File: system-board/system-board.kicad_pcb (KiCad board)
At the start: 4 copper layers, 50 x 17.5 mm, 69 parts, among them IC1 Flash_16Mb, IC2 LSM6DSLTR, IC3 AP2115M-3.3TRG1, J1 BATT, J10 217183-0001, J2 GTFP08431BEU, J3 QWIIC, J4 SPKR, J5 BLADE_1, J6 BLADE_2, J7 BLADE_3, J8 BLADE_4, J9 BTNS, Q1 DMP1012UFDF, Q2 SSM6K504NU.LF, Q3 SSM6K504NU.LF, Q4 DMP1012UFDF, Q5 PMZB290UNE2YL, Q6 PMZB290UNE2YL, Q7 PMZB290UNE2YL, Q8 PMZB290UNE2YL, SW1 RST, SW2 USR, U1 MDBT50Q-1MV2, U2 MAX98357AETE+T, U3 BQ29705DSER, U4 MCP73832-2-OT, Y1 32.768k

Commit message: First attempt
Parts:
- removed J5: BLADE_1, Connector_JST:JST_SH_SM02B-SRSS-TB_1x02-1MP_P1.00mm_Horizontal
- removed J6: BLADE_2, Connector_JST:JST_SH_SM02B-SRSS-TB_1x02-1MP_P1.00mm_Horizontal
- removed J7: BLADE_3, Connector_JST:JST_SH_SM02B-SRSS-TB_1x02-1MP_P1.00mm_Horizontal
- removed J8: BLADE_4, Connector_JST:JST_SH_SM02B-SRSS-TB_1x02-1MP_P1.00mm_Horizontal
- added J11: 503398-1892, Imports:Molex uSD Card Holder Push-Push 503398-1892, B.Cu at (116.8, 91.4)
- C1, C2, C3, C4, C5, C6, C7, C8, FB1, FB2, R1, R2, R7, U1, Y1: moved to B.Cu
- D1: value WS2812B -> WS2812B-2020
- IC2, J3, R5, R6: moved to F.Cu
- J2: value GTFP08431BEU -> LEDs; footprint Imports:GTFP08431BEU -> Connector_PinSocket_2.00mm:PinSocket_2x04_P2.00mm_Vertical; moved to F.Cu
- J4: footprint Connector_JST:JST_SH_SM02B-SRSS-TB_1x02-1MP_P1.00mm_Horizontal -> Connector_PinSocket_2.00mm:PinSocket_1x02_P2.00mm_Vertical
- J9: value BTNS -> BTNs; footprint Connector_JST:JST_SH_SM05B-SRSS-TB_1x05-1MP_P1.00mm_Horizontal -> Connector_PinSocket_2.00mm:PinSocket_2x03_P2.00mm_Vertical; moved to F.Cu
- U2: footprint MaximCustom:Maxim_Integrated-T1633-4-0-V-IPC_C -> Imports:Maxim_Integrated-T1633-4-0-V-IPC_C; moved to B.Cu
- moved J3 44.4 mm to (72.2, 98.2), turned to -90 degrees
- moved R6 42.5 mm to (76.3, 101.1), turned to -90 degrees
- moved R5 40.2 mm to (76.3, 98.2), turned to -90 degrees
- moved C6 36.8 mm to (82.6, 95.0), turned to 90 degrees
- moved J4 34.5 mm to (83.2, 92.6)
- moved FB2 33.4 mm to (84.5, 94.8), turned to 0 degrees
- moved Q5 31.5 mm to (85.1, 99.9), turned to -90 degrees
- moved FB1 30.5 mm to (88.2, 91.8), turned to 0 degrees
- moved C5 30.4 mm to (87.6, 93.1), turned to 180 degrees
- moved IC3 28.7 mm to (79.6, 100.8), turned to -90 degrees
- moved R15 25.3 mm to (79.6, 105.0), turned to 180 degrees
- moved C11 25.2 mm to (82.0, 105.3)
- moved SW1 24.8 mm to (70.1, 92.8), turned to 0 degrees
- moved Q6 23.7 mm to (87.1, 99.9), turned to -90 degrees
- moved C12 23.3 mm to (83.1, 98.0), turned to -90 degrees
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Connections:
- J2 pad 1: unconnected-(J2-DAT2-Pad1) -> /Blade LED Out/Blade_1_Out
- J2 pad 2: GND -> VDD
- J2 pad 3: /MOSI -> /Blade LED Out/Blade_2_Out
- J2 pad 4: VCC -> VDD
- J2 pad 5: /SCK -> /Blade LED Out/Blade_3_Out
- J2 pad 6: GND -> VDD
- J2 pad 7: /MISO -> /Blade LED Out/Blade_4_Out
- J2 pad 8: unconnected-(J2-DAT1-Pad8) -> VDD
- J9 pad 2: /A0 -> GND
- J9 pad 3: Net-(J9-Pin_3) -> /A0
- J9 pad 4: Net-(J9-Pin_4) -> /A2
- J9 pad 5: /A2 -> Net-(J9-Pin_5)
- R21 pad 1: Net-(J9-Pin_3) -> Net-(J9-Pin_5)
- R22 pad 1: Net-(J9-Pin_4) -> Net-(J9-Pin_6)
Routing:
- net /D10: track 54.1 -> 0.00 mm, vias 3 -> 0
- net /D9: track 47.4 -> 0.00 mm, vias 1 -> 0
- net /SCL: track 49.1 -> 4.41 mm, vias 3 -> 1
- net /SDA: track 48.1 -> 5.53 mm
- net /D6: track 36.1 -> 0.00 mm, vias 1 -> 0
- net /D5: track 35.7 -> 0.00 mm, vias 1 -> 0
- net /CONN_USB_D+: track 24.4 -> 50.0 mm, vias 2 -> 1
- net /CONN_USB_D-: track 24.6 -> 48.3 mm, vias 2 -> 1
- net /A0: track 21.7 -> 0.00 mm, vias 1 -> 0
- net /Power Management/BATT_PROT_+: track 4.20 -> 25.2 mm
- net /VDIV: track 40.1 -> 20.0 mm, vias 2 -> 1
- net /Power Management/VBUS: track 51.6 -> 69.6 mm, vias 3 -> 5
- net GND: track 107.9 -> 90.6 mm, vias 34 -> 30
- net Net-(J10-CC2): track 0.89 -> 16.0 mm, vias 0 -> 1
- net /A4: track 28.5 -> 15.6 mm, vias 2 -> 1
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- removed copper zone on F.Cu, net /Power Management/BATT_PROT_+
- removed copper zone on F.Cu, net /Power Management/BATT_RAW_+
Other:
- board size 50 x 17.5 mm -> 50 x 15 mm
- board text removed: "+"
- board text removed: "-"

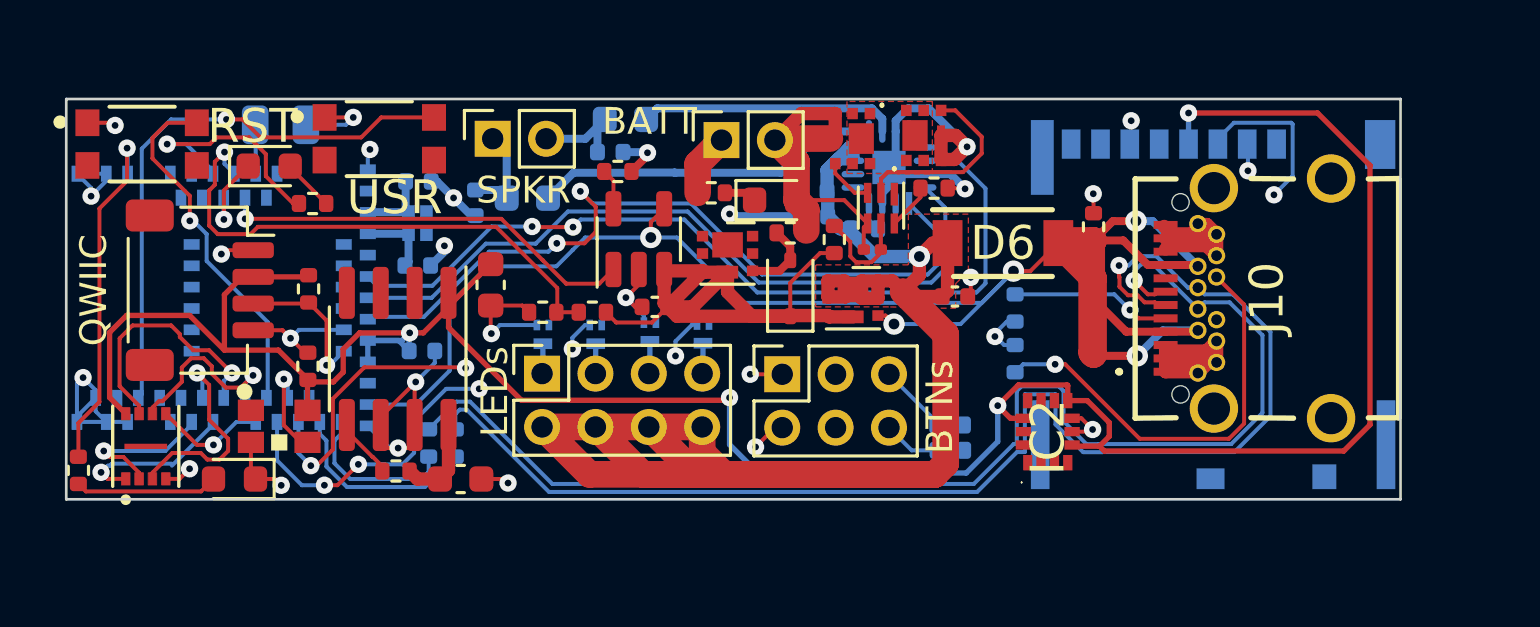
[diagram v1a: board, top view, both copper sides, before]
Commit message: Redo system-board PCB to use fewer connectors
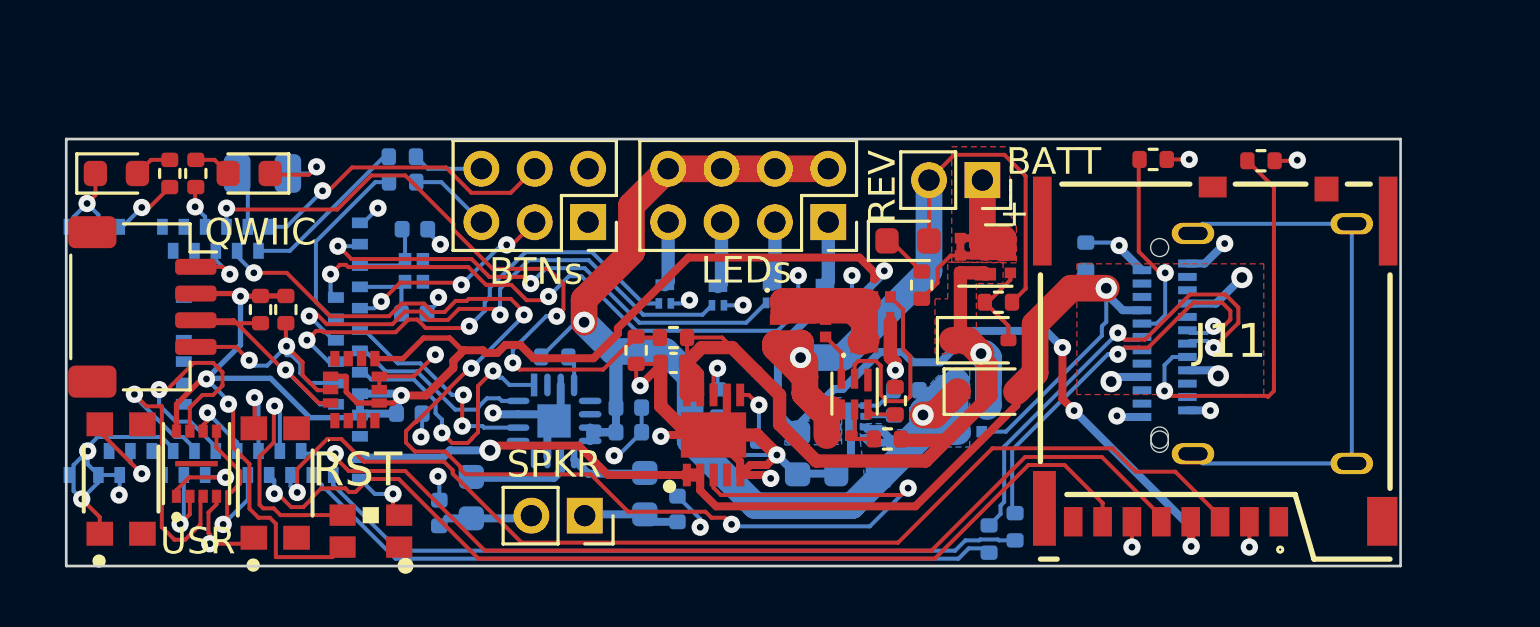
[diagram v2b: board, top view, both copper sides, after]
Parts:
- removed J10: 217183-0001, Imports:Molex USB-C Horizontal 2171830001
- removed U4: MCP73832-2-OT, Package_TO_SOT_SMD:SOT-23-5
- added IC4: MCP73834T-FCI_MF, Imports:SON50P300X300X100-11N-D, F.Cu at (91.5, 103.7)
- added J5: 105450-0101, Imports:AMPHENOL_12401832E402A, B.Cu at (108.2, 100.2)
- added R17: 10k, Resistor_SMD:R_0402_1005Metric, B.Cu at (91.7, 102.5)
- C11, C12, C15, Q4, R11, R15, R16: moved to B.Cu
- D6: value RSX501LAM20TR -> PMEG1030EJ; footprint Imports:SODFL4725X105N -> Diode_SMD:D_SOD-323F
- IC3: value AP2115M-3.3TRG1 -> NCP186AMX330TAG; footprint Package_SO:SOIC-8_3.9x4.9mm_P1.27mm -> Imports:NCP186AMX330TAG; moved to B.Cu
- J11, R23, R24: moved to F.Cu
- moved IC2 26.0 mm to (78.0, 102.0)
- moved R22 23.3 mm to (79.8, 93.2), turned to 180 degrees
- moved R21 22.4 mm to (79.8, 94.2), turned to 180 degrees
- moved R1 22.2 mm to (102.8, 107.1)
- moved R2 20.3 mm to (101.8, 107.6)
- moved R15 18.7 mm to (98.3, 103.4), turned to 90 degrees
- moved J11 17.0 mm to (116.8, 108.3)
- moved IC3 16.9 mm to (96.4, 103.2), turned to 90 degrees
- moved SW2 16.0 mm to (69.3, 105.3), turned to 90 degrees
- moved U2 15.7 mm to (85.5, 103.1), turned to -90 degrees
- moved FB1 15.3 mm to (82.4, 106.0), turned to 90 degrees
- moved C5 15.0 mm to (81.2, 106.6), turned to -90 degrees
- moved C11 14.9 mm to (96.9, 105.1), turned to 180 degrees
- moved J4 14.5 mm to (86.7, 106.7), turned to -90 degrees
- moved C6 13.7 mm to (90.1, 106.4), turned to -90 degrees
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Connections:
- net Net-(U3-BAT) renamed /Power Management/BATT_FILTERED
- IC3 pad 2: unconnected-(IC3-NC_1-Pad2) -> VCC
- IC3 pad 4: unconnected-(IC3-NC_3-Pad4) -> VCC
- IC3 pad 5: Net-(IC3-EN) -> GND
- IC3 pad 6: GND -> /Power Management/VREG_EN
- IC3 pad 7: GND -> VDD
- R15 pad 2: Net-(IC3-EN) -> /Power Management/VREG_EN
- R23 pad 1: Net-(J10-CC2) -> /USB Connector/CC1
- R24 pad 1: Net-(J10-CC1) -> /USB Connector/CC2
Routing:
- net /SCK: track 0.00 -> 36.2 mm, vias 0 -> 1
- net VDD: track 89.3 -> 55.4 mm, vias 1 -> 2
- net /A4: track 15.6 -> 48.0 mm, vias 1 -> 5
- net /CONN_USB_D-: track 48.3 -> 16.1 mm, vias 1 -> 2
- net /CONN_USB_D+: track 50.0 -> 18.8 mm, vias 1 -> 2
- net /MISO: track 11.6 -> 36.6 mm, vias 3 -> 1
- net /MOSI: track 16.3 -> 41.1 mm, vias 3 -> 1
- net /D11: track 31.9 -> 8.04 mm
- net /D9: track 0.00 -> 21.6 mm, vias 0 -> 2
- net unconnected-(J5-SHIELD-PadS1): track 0.00 -> 21.2 mm
- net /MCU_USB_D-: track 6.11 -> 27.1 mm
- net /D12: track 27.7 -> 6.88 mm
- net /D6: track 0.00 -> 19.6 mm, vias 0 -> 2
- net /Power Management/VBUS: track 69.6 -> 50.0 mm
- net /MCU_USB_D+: track 7.40 -> 26.8 mm
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- added copper zone on F.Cu, net /Power Management/BATT_PROT_+
- added copper zone on F.Cu, net /Power Management/BATT_RAW_+
- added copper zone on F.Cu, net /Power Management/VBUS
- added copper zone on B.Cu, net VCC
- added copper zone on B.Cu, net VDD
- removed copper zone on F.Cu, net Net-(Q2-D)
- removed copper zone on F.Cu, net VDD
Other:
- board size 50 x 15 mm -> 50 x 16 mm
- board text added: "+"
- board text added: "-"

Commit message: Yet another PCB Revision
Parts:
- added IC5: HSP061-2M6, Imports:SON50P100X145X65-6N-D, B.Cu at (104.1, 103.9)
- added J6: DBG, Imports:Prog-Pads, B.Cu at (72.7, 107.2)
- moved R2 1.57 mm to (103.3, 107.2)
- moved R1 1.57 mm to (104.3, 106.8)
- moved J3 0.28 mm to (70.4, 98.8)
- moved IC1 0.23 mm to (72.1, 104.5)
- moved C5 0.18 mm to (81.2, 106.4), turned to 90 degrees
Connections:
- J5 pad A6: /CONN_USB_D+ -> /USB Connector/RAW_D+
- J5 pad A7: /CONN_USB_D- -> /USB Connector/RAW_D-
- J5 pad B6: /CONN_USB_D+ -> /USB Connector/RAW_D+
- J5 pad B7: /CONN_USB_D- -> /USB Connector/RAW_D-
- U1 pad 47: GND -> /SW0
- U1 pad 51: GND -> /SWDIO
- U1 pad 53: GND -> /SWCLK
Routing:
- net /USB Connector/RAW_D+: track 0.00 -> 15.1 mm, vias 0 -> 2
- net /CONN_USB_D-: track 16.1 -> 1.98 mm, vias 2 -> 0
- net /SW0: track 0.00 -> 13.1 mm, vias 0 -> 2
- net /USB Connector/RAW_D-: track 0.00 -> 12.2 mm, vias 0 -> 2
- net /CONN_USB_D+: track 18.8 -> 7.33 mm, vias 2 -> 0
- net /NEOPIX: track 8.97 -> 15.2 mm, vias 1 -> 3
- net /MCU_USB_D+: track 26.8 -> 31.0 mm
- net /Power Management/VBUS: track 50.0 -> 53.1 mm, vias 5 -> 6
- net /SWDIO: track 0.00 -> 2.60 mm
- net /SCK: track 36.2 -> 38.8 mm
- net /QSPI_D0: track 6.46 -> 4.15 mm
- net /MCU_USB_D-: track 27.1 -> 29.3 mm
- net /SWCLK: track 0.00 -> 1.75 mm
- net /QSPI_D1: track 3.09 -> 4.79 mm
- net /SWITCH: track 3.25 -> 1.62 mm
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
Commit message: Redo design again
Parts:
- removed the IC2 at (78.0, 102.0)
- removed the IC3 at (96.4, 103.2)
- removed the J3 at (70.4, 98.8)
- removed the R5 at (74.5, 99.0)
- removed the R6 at (75.5, 99.0)
- added C14: 0.1 uF, Capacitor_SMD:C_0402_1005Metric, F.Cu at (87.5, 103.4)
- added C15: 0.1 uF, Capacitor_SMD:C_0402_1005Metric, F.Cu at (89.4, 103.4)
- added C16: 0.1 uF, Capacitor_SMD:C_0402_1005Metric, F.Cu at (91.2, 100.8)
- added IC4: ICM-20648, Imports:QFN40P300X300X95-25N-D, F.Cu at (88.6, 100.8)
- added J8: QWIIC, Connector_JST:JST_SH_SM04B-SRSS-TB_1x04-1MP_P1.00mm_Horizontal, F.Cu at (72.2, 98.7)
- added R20: 2.0k, Resistor_SMD:R_0402_1005Metric, F.Cu at (77.2, 98.6)
- added R21: 2.0k, Resistor_SMD:R_0402_1005Metric, F.Cu at (78.2, 98.6)
- added U4: TLV75733PDRV, Package_SON:WSON-6-1EP_2x2mm_P0.65mm_EP1x1.6mm, B.Cu at (97.2, 103.5)
- C10: footprint Capacitor_SMD:C_0201_0603Metric -> Capacitor_SMD:C_0402_1005Metric
- C11, C12: footprint Capacitor_SMD:C_0603_1608Metric -> Capacitor_SMD:C_0402_1005Metric
- IC1: footprint Imports:USON-8-03x02mm-PSON50P200X300X50-9N -> Package_SO:SOP-8_3.9x4.9mm_P1.27mm
- J2: renamed from J11; moved to B.Cu
- J7: renamed from J5; moved to F.Cu
- R10: moved to B.Cu
- R11: renamed from R12; moved to B.Cu
- R14: renamed from R16; moved to F.Cu
- R8: renamed from R11; moved to F.Cu
- R9: renamed from R17; moved to F.Cu
- moved J2 13.4 mm to (103.5, 107.5), turned to 0 degrees
- moved R9 12.5 mm to (104.1, 104.0)
- moved SW1 11.5 mm to (78.5, 94.5), turned to 180 degrees
- moved IC1 10.8 mm to (82.4, 101.2), turned to 180 degrees
- moved R8 10.6 mm to (103.2, 104.0), turned to -90 degrees
- moved C9 10.2 mm to (100.1, 99.8), turned to 0 degrees
- moved IC2 8.76 mm to (100.2, 102.7)
- moved R19 6.89 mm to (105.5, 95.6), turned to 90 degrees
- moved R1 6.51 mm to (97.8, 106.8), turned to 180 degrees
- moved C10 6.03 mm to (98.8, 98.2), turned to 90 degrees
- moved R12 5.96 mm to (94.2, 104.2), turned to -90 degrees
- moved R13 5.95 mm to (93.2, 104.2), turned to 90 degrees
- moved R6 5.57 mm to (100.2, 98.7)
- moved R2 5.56 mm to (97.8, 107.7), turned to 180 degrees
- moved D6 5.45 mm to (96.7, 104.2)
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- renumbered C15 to C13, IC4 to IC2, IC5 to IC3, J6 to J3, J2 to J5, J9 to J6, R13 to R12, R14 to R13, R22 to R16, R21 to R17, R23 to R18, R24 to R19, R7 to R5, R8 to R6, R9 to R7
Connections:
- IC3 pad 1: /CONN_USB_D- -> /CONN_USB_D+
- IC3 pad 3: /CONN_USB_D+ -> /CONN_USB_D-
- IC3 pad 4: /USB Connector/RAW_D+ -> /USB Connector/RAW_D-
- IC3 pad 6: /USB Connector/RAW_D- -> /USB Connector/RAW_D+
- R15 pad 1: VDD -> Net-(U4-EN)
- R15 pad 2: /Power Management/VREG_EN -> VDD
- U2 pad 1: /D13 -> /D11
- U2 pad 14: /D11 -> /D13
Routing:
- net VDD: track 55.4 -> 18.7 mm, vias 2 -> 1
- net /Power Management/BATT_PROT_+: track 37.6 -> 6.50 mm
- net VCC: track 93.3 -> 118.8 mm, vias 8 -> 7
- net /Power Management/BATT_RAW_-: track 30.8 -> 6.40 mm
- net /Power Management/VBUS: track 53.1 -> 31.7 mm, vias 6 -> 8
- net /QSPI_D0: track 4.15 -> 21.5 mm, vias 1 -> 5
- net /SCL: track 10.3 -> 25.2 mm, vias 2 -> 3
- net /RESET: track 3.06 -> 17.4 mm
- net /NEOPIX: track 15.2 -> 1.45 mm, vias 3 -> 1
- net /Power Management/BATT_FILTERED: track 1.58 -> 14.4 mm
- net /QSPI_D1: track 4.79 -> 16.7 mm, vias 1 -> 3
- net /QSPI_CS: track 2.98 -> 14.6 mm, vias 1 -> 3
- net Net-(Q2-D): track 11.4 -> 0.00 mm
- net /D5: track 17.2 -> 27.5 mm, vias 2 -> 4
- net /SDA: track 11.1 -> 21.3 mm
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- added copper zone on B.Cu, net /Power Management/BATT_PROT_+
- added copper zone on F.Cu, net /Power Management/BATT_RAW_-
- added copper zone on B.Cu, net /Power Management/VBUS
- added copper zone on F.Cu, net Net-(Q2-D)
- removed copper zone on B.Cu, net VCC
